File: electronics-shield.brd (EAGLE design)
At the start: 132 x 70 mm, 5 parts

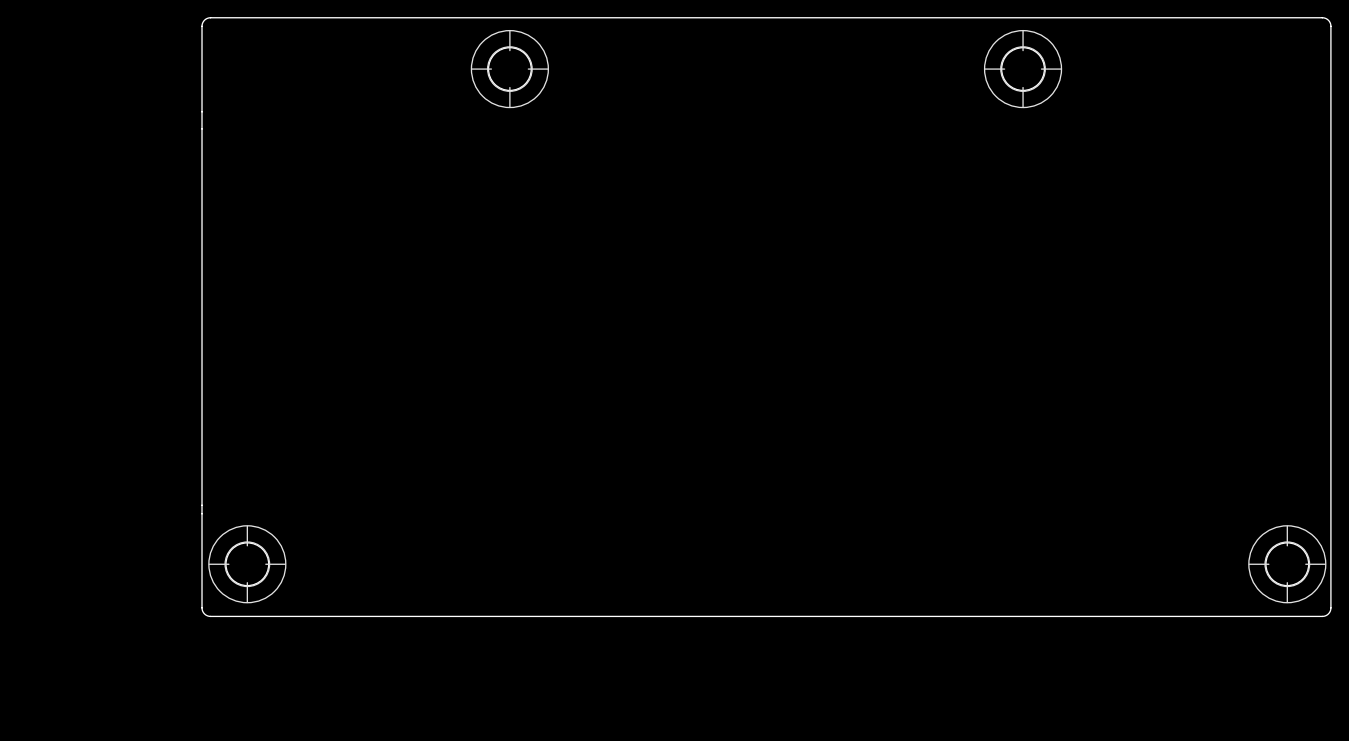
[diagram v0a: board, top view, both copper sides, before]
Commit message: H-Bridge change from L298P to TLE9201S, better wiring
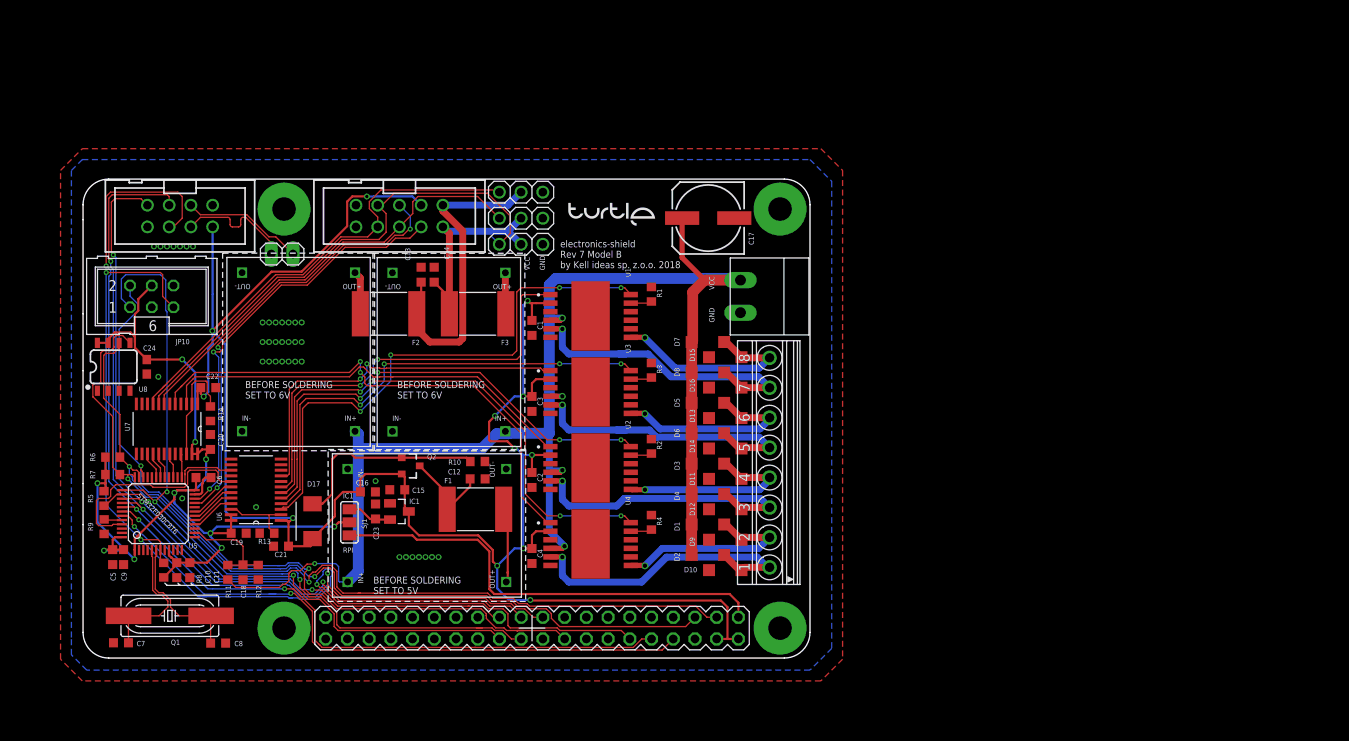
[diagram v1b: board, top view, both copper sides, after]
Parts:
- removed U$2: (no value), FIBOX:AB_081607
- removed U$3, U$4, U$5, U$6: (no value), holes:5,0
- added C1, C11, C12, C13, C14, C19, C2, C20, C21, C22, C23, C3, C4, C6, C9: 100n, resistor:C0603K
- added C10: 1u, resistor:C0603K
- added C15: 4.7uF, resistor:C0603K
- added C16: 1uF, resistor:C0603K
- added C17: 100u, resistor:153CLV-0807
- added C18: 22u, resistor:C0603K
- added C24: 0.1uF, rcl:C0603
- added C5: 4u7, resistor:C0603K
- added C7, C8: 20p, resistor:C0603K
- added D1, D10, D11, D12, D13, D14, D15, D16, D2, D3, D4, D5, D6, D7, D8, D9: SK38SMA, diode:SOD123
- added D17: SMBJ5.0A-TR, diode:SMBJ
- added F1, F2, F3: SL125-33, polyfuse-smd_10:2920L
- added IC1: MCP1703CB, linear:SOT23
- added JP1: Listwa kołkowa 2.54mm prosta 1x2 (2pin), pinhead:1X02
- added JP10: gniazdo IDC męskie 6pin proste, con-harting-ml:ML6
- added JP2, JP3, JP4: Listwa kołkowa 2.54mm prosta 1x3 (3pin), Synergiczne:1X03
- added JP5: Listwa stykowa 2.54mm prosta 2x20 (40-pin), wydłużona, RASPBERRY_PI_Bplus-eagle5:2X20
- added JP6: gniazdo IDC męskie 10pin proste, con-3m:PAK100/2500-10
- added JP7: gniazdo IDC męskie 8pin proste, Simplex-Connectors:PAK100/2500-10
- added JP8: Listwa zaciskowa rozłączalna 3.81mm 2pin kątowe 90° gniazdo, con-phoenix-381_l:MC2
- added JP9: Listwa zaciskowa rozłączalna 3.50mm 8pin kątowe 90° gniazdo, con-phoenix-350:1751303
- added PCB1, PCB2, PCB3: Moduł przetwornicy DC-DC Step-down 4.5..28V --- regulowane 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, Kell Ideas:MP1584_MODULE
- added Q1: 8 MHz, crystal:HC49UP
- added Q2: MOSFET-PCHANNELSMD, User-Submitted:SOT23-3
- added R1, R2, R3, R4: 10k, rcl:R0603
- added R10: 100k, rcl:R0603
- added R11, R13, R14, R5, R8, R9: 10k, resistor:R0603
- added R12: 1k, resistor:R0603
- added R6, R7: 4k7, resistor:R0603
- added SJ1: Zworka cynowa, jumper:SJ_2
- added U1, U2, U3, U4: TLE9201SGAUMA1, Kell Ideas:PG-DSO-12-9
- added U5: STM32F051C8T, STM32F030:LQFP48
- added U6, U7: SN74LVC4245APWR, Texas Instruments_By_element14_Batch_1:SOP65P640X120-24N
- added U8: 24LC256, SparkFun-IC-Memory:SO08
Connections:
- new net +3V3: C10.1, C11.1, C19.1, C20.1, C24.1, C5.1, C6.1, C9.1, JP10.4, R5.2, R6.2, R7.2, R8.2, SJ1.2, U5.1, U5.24, U5.48, U5.9, U6.23, U6.24, U7.23, U7.24, U8.7, U8.8
- new net +5V: C1.1, C15.1, C2.1, C21.1, C22.1, C23.1, C3.1, C4.1, D17.C, IC1.3, JP5.2, JP5.4, JP6.3, JP7.2, Q2.2, U1.2, U2.2, U3.2, U4.2, U6.1, U7.1
- new net +5V_RAW: F1.2, PCB1.OUT1+1
- new net +7V/1: C13.1, F2.1, JP4.2, JP6.1
- new net +7V/1_RAW: F2.2, PCB2.OUT1+1
- new net +7V/2: C14.1, F3.2, JP2.2, JP3.2, JP6.2
- new net +7V/2_RAW: F3.1, PCB3.OUT1+1
- new net 3V3: JP5.17
- new net 3V3_RPI: JP5.1, SJ1.3
- new net 3V3_STABILIZED: C16.1, IC1.2, SJ1.1
- new net 5V_NOT_TRIMMED: C12.1, F1.1, Q2.3
- new net BAT_MEAS: C18.1, R11.1, R12.2, U5.14
- new net BOOT0: R9.2, U5.44
- new net D1-R3: D17.A, Q2.1, R10.2
- new net DATA_N: JP1.2, JP7.3
- new net DATA_P: JP1.1, JP7.4
- new net EN1: U1.12, U6.3
- new net EN1_UC: U5.16, U6.21
- new net EN2: U3.12, U6.4
- new net EN2_UC: U5.17, U6.20
- new net EN3: U2.12, U6.5
- new net EN3_UC: U5.18, U6.19
- new net EN4: U4.12, U6.6
- new net EN4_UC: U5.19, U6.18
- new net GND: C1.2, C10.2, C11.2, C12.2, C13.2, C14.2, C15.2, C16.2, C17.-, C18.2, C19.2, C2.2, C20.2, C21.2, C22.2, C23.2, C24.2, C3.2, C4.2, C5.2, C6.2, C7.1, C8.1, C9.2, D10.A, D11.A, D12.A, D13.A, D14.A, D15.A, D16.A, D9.A, IC1.1, JP10.3, JP2.3, JP3.3, JP4.3, JP5.14, JP5.20, JP5.25, JP5.30, JP5.34, JP5.39, JP5.6, JP5.9, JP6.10, JP6.9, JP7.1, JP7.8, JP8.1, PCB1.IN1-1, PCB1.OUT1-1, PCB2.IN1-1, PCB2.OUT1-1, PCB3.IN1-1, PCB3.OUT1-1, R1.1, R10.1, R12.1, R13.2, R14.2, R2.1, R3.1, R4.1, R9.1, U1.13, U1.6, U2.13, U2.6, U3.13, U3.6, U4.13, U4.6, U5.23, U5.47, U5.8, U6.11, U6.12, U6.13, U7.11, U7.12, U7.13, U8.2, U8.3, U8.4
- new net IN11: U1.1, U6.7
- new net IN11_UC: U5.45, U6.17
- new net IN12: U6.8
- new net IN12_UC: U6.16
- new net IN21: U3.1, U6.9
- new net IN21_UC: U5.32, U6.15
- new net IN22: U6.10
- new net IN22_UC: U6.14
- new net IN31: U2.1, U7.3
- new net IN31_UC: U5.25, U7.21
- new net IN32: U7.4
- new net IN32_UC: U7.20
- new net IN41: U4.1, U7.5
- new net IN41_UC: U5.27, U7.19
- new net IN42: U7.6
- new net IN42_UC: U7.18
- new net LED: U5.15
- new net MOT11: D16.C, D8.A, JP9.7, U1.5
- new net MOT12: D15.C, D7.A, JP9.8, U1.7
- new net MOT21: D14.C, D6.A, JP9.5, U3.5
- new net MOT22: D13.C, D5.A, JP9.6, U3.7
- new net MOT31: D12.C, D4.A, JP9.3, U2.5
- new net MOT32: D11.C, D3.A, JP9.4, U2.7
- new net MOT41: D10.C, D2.A, JP9.1, U4.5
- new net MOT42: D1.A, D9.C, JP9.2, U4.7
- new net N$1: R13.1, U6.2, U6.22
- new net N$2: R14.1, U7.2, U7.22
- new net N$3: U7.10
- new net N$4: U7.14
- new net N$8: JP10.6
- new net NRST: JP10.5, JP5.12, R8.1, U5.7
- new net OSCILATOR_N: C7.2, Q1.2, U5.5
- new net OSCILATOR_P: C8.2, Q1.1, U5.6
- new net RPI_CLK: JP5.23, JP7.7, U5.39
- new net RPI_MISO: JP5.21, JP7.5, U5.40
- new net RPI_MOSI: JP5.19, JP7.6, U5.41
- new net RPI_RXD: JP5.10, U5.42
- new net RPI_TXD: JP5.8, U5.43
- new net SCL: JP5.5, R7.1, U5.35, U8.6
- new net SCL_TX: JP6.5, U5.21
- new net SDA: JP5.3, R6.1, U5.36, U8.5
- new net SDA_RX: JP6.4, U5.22
- new net SEN1: U5.10
- new net SEN2: U5.11
- new net SEN3: U5.12
- new net SEN4: U5.13
- new net SERVO1: JP2.1, JP6.6, U7.7
- new net SERVO1_UC: U5.29, U7.17
- new net SERVO2: JP3.1, JP6.7, U7.8
- new net SERVO2_UC: U5.30, U7.16
- new net SERVO3: JP4.1, JP6.8, U7.9
- new net SERVO3_UC: U5.31, U7.15
- new net SPI1_NSS: JP5.24, R5.1, U5.38
- new net SWCLK: JP10.1, JP5.22, U5.37
- new net SWDIO: JP10.2, JP5.18, U5.34
- new net U5_DIS: R1.2, U1.11
- new net U6_DIS: R2.2, U2.11
- new net U7_DIS: R3.2, U3.11
- new net U8_DIS: R4.2, U4.11
- new net VCC: C17.+, D1.C, D2.C, D3.C, D4.C, D5.C, D6.C, D7.C, D8.C, JP8.2, PCB1.IN1+1, PCB2.IN1+1, PCB3.IN1+1, R11.2, U1.4, U2.4, U3.4, U4.4
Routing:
- net +5V: track 0.00 -> 225.1 mm, vias 0 -> 12
- net VCC: track 0.00 -> 212.5 mm, vias 0 -> 5
- net NRST: track 0.00 -> 120.4 mm, vias 0 -> 3
- net +3V3: track 0.00 -> 119.9 mm, vias 0 -> 10
- net RPI_MOSI: track 0.00 -> 110.6 mm, vias 0 -> 3
- net SDA: track 0.00 -> 103.8 mm, vias 0 -> 2
- net RPI_MISO: track 0.00 -> 100.3 mm, vias 0 -> 3
- net SCL: track 0.00 -> 96.9 mm, vias 0 -> 2
- net SWCLK: track 0.00 -> 92.8 mm, vias 0 -> 3
- net RPI_CLK: track 0.00 -> 91.2 mm, vias 0 -> 3
- net SWDIO: track 0.00 -> 88.0 mm, vias 0 -> 2
- net RPI_TXD: track 0.00 -> 74.9 mm, vias 0 -> 2
- net RPI_RXD: track 0.00 -> 71.6 mm, vias 0 -> 2
- net EN1: track 0.00 -> 64.4 mm, vias 0 -> 4
- net EN4: track 0.00 -> 63.9 mm, vias 0 -> 4
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- added copper zone on layer 1, net GND
- added copper zone on layer 16, net GND
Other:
- board size 132 x 70 mm -> 85 x 56 mm
- board text added: "+5V"
- board text added: "+7V/1"
- board text added: "+7V/2"
- board text added: "3v3"
- board text added: "BEFORE SOLDERING SET TO 5V"
- board text added: "BEFORE SOLDERING SET TO 6V"
- board text added: "CLK"
- board text added: "DATA+"
- board text added: "DATA-"
- board text added: "GND"
- board text added: "IC1"
- board text added: "M11"
- board text added: "M12"
- board text added: "M21"
- board text added: "M22"
- board text added: "M31"
- board text added: "M32"
- board text added: "M41"
- board text added: "M42"
- board text added: "MISO"
- board text added: "MOSI"
- board text added: "MOTOR CONNECTOR"
- board text added: "NC"
- board text added: "NRST"
- board text added: "PiHat Rev. 7"
- board text added: "Power connector"
- board text added: "RPI"
- board text added: "SCL/TX"
- board text added: "SDA/RX"
- board text added: "SERVO1"
- board text added: "SERVO2"
- board text added: "SERVO3"
- board text added: "SIG"
- board text added: "STM32F030C8T6"
- board text added: "SWCLK"
- board text added: "SWDIO"
- board text added: "TIM1"
- board text added: "TIM2"
- board text added: "TIM3"
- board text added: "VCC"
- board text added: "electronics-shield Rev 7 Model B by Kell ideas sp. z.o.o. 2018"

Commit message: changed base for 7.c
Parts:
- removed C21, C22, C23: 100n, resistor:C0603K
- removed C24: 0.1uF, rcl:C0603
- removed JP10: gniazdo IDC męskie 6pin proste, con-harting-ml:ML6
- removed JP4: Listwa kołkowa 2.54mm prosta 1x3 (3pin), Synergiczne:1X03
- removed JP5: Listwa stykowa 2.54mm prosta 2x20 (40-pin), wydłużona, RASPBERRY_PI_Bplus-eagle5:2X20
- removed JP6: gniazdo IDC męskie 10pin proste, con-3m:PAK100/2500-10
- removed JP7: gniazdo IDC męskie 8pin proste, Simplex-Connectors:PAK100/2500-10
- removed JP8: Listwa zaciskowa rozłączalna 3.81mm 2pin kątowe 90° gniazdo, con-phoenix-381_l:MC2
- removed JP9: Listwa zaciskowa rozłączalna 3.50mm 8pin kątowe 90° gniazdo, con-phoenix-350:1751303
- removed PCB2, PCB3: Moduł przetwornicy DC-DC Step-down 4.5..28V --- regulowane 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, Kell Ideas:MP1584_MODULE
- removed R14: 10k, resistor:R0603
- removed U5: STM32F051C8T, STM32F030:LQFP48
- removed U6, U7: SN74LVC4245APWR, Texas Instruments_By_element14_Batch_1:SOP65P640X120-24N
- removed U8: 24LC256, SparkFun-IC-Memory:SO08
- added $3_0_$_2018-08-14_21-12-08, $3_1_$_2018-08-14_21-12-08, $3_2_$_2018-08-14_21-12-08: Moduł przetwornicy DC-DC Step-down 4.5..28V --- regulowane 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, Kell Ideas:DC-BRICK
- added IC2: TLE9201SG, Kell Ideas:PG-DSO-12-9
- added IC5: LINEAR_MCP1703CB, electronics-shield:LINEAR_SOT23
- added J1: USB-MICRO-B, Kell Ideas:USB-MICRO-B
- added LED1, LED2, LED3, LED4, LED5: LEDCHIPLED_0603, audio amplifier example:CHIPLED_0603
- added Q3: ON-SEMICONDUCTOR---NTZD3154NT1G_ON_SEMICONDUCTOR_NTZD3154NT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, electronics-shield:ON-SEMICONDUCTOR---NTZD3154NT1G_ON_SEMICONDUCTOR_NTZD3154NT1G_0
- added RN1, RN2: 1k, SparkFun-Resistors:0805-ARV
- added SJ2: (no value), Kell Ideas:SJ
- added SV1: gniazdo IDC męskie 6pin proste, Kell Ideas:ML6
- added SV2: (no value), Kell Ideas:ML10
- added SV3: ML8, Kell Ideas:ML8
- added X1: CONNECTOR_PHOENIX_3.81, Kell Ideas:3.81MM_2PIN
- added X2: Listwa zaciskowa rozłączalna 3.50mm 8pin kątowe 90° gniazdo, Kell Ideas:3.5MM_8PIN
- added Y1: 8 MHz, Kell Ideas:HC49UP
- C1, C10, C11, C12, C13, C14, C15, C16, C18, C19, C2, C3, C4, C5, C6, C7, C8, C9: device resistor:C0603K -> Kell Ideas:C0603K
- C17: device resistor:153CLV-0807 -> Kell Ideas:FI8_6.2
- C20: value 100n -> 0.1uF; device resistor:C0603K -> Kell Ideas:C0603K
- D1, D10, D11, D12, D13, D14, D15, D16, D2, D3, D4, D5, D6, D7, D8, D9: device diode:SOD123 -> Kell Ideas:SOD123
- D17: device diode:SMBJ -> Kell Ideas:SMBJ
- F1, F2, F3: device polyfuse-smd_10:2920L -> Kell Ideas:FUSC7351X125
- IC1: value MCP1703CB -> TLE9201SG; device linear:SOT23 -> Kell Ideas:PG-DSO-12-9
- IC3, IC4: value TLE9201SGAUMA1 -> TLE9201SG
- JP1: value Listwa kołkowa 2.54mm prosta 1x2 (2pin) -> Listwa kołkowa 2.54mm prosta 1x3 (3pin); device pinhead:1X02 -> Kell Ideas:1X03_ROUND_DNP
- JP2, JP3: device Synergiczne:1X03 -> Kell Ideas:1X03_ROUND_DNP
- PCB1: value Moduł przetwornicy DC-DC Step-down 4.5..28V --- regulowane 0.8..20V MP1584 -> Listwa stykowa 2.54mm prosta 2x20 (40-pin), wydłużona; device Kell Ideas:MP1584_MODULE -> Kell Ideas:RASPBERRY_PI_B+_CONNECTOR
- Q1: value 8 MHz -> USER-SUBMITTED_MOSFET-PCHANNELSMD; device crystal:HC49UP -> electronics-shield:USER-SUBMITTED_SOT23-3
- Q2: value MOSFET-PCHANNELSMD -> ON-SEMICONDUCTOR---NTZD3154NT1G_ON_SEMICONDUCTOR_NTZD3154NT1GON_SEMICONDUCTOR_NTZD3154NT1G_0_0; device User-Submitted:SOT23-3 -> electronics-shield:ON-SEMICONDUCTOR---NTZD3154NT1G_ON_SEMICONDUCTOR_NTZD3154NT1G_0
- R1, R4: device rcl:R0603 -> Kell Ideas:R0603
- R10: value 100k -> 330; device rcl:R0603 -> Kell Ideas:R0603
- R11: value 10k -> 330; device resistor:R0603 -> Kell Ideas:R0603
- R12: value 1k -> 200; device resistor:R0603 -> Kell Ideas:R0603
- R13: value 10k -> 200; device resistor:R0603 -> Kell Ideas:R0603
- R2, R3: value 10k -> 4k7; device rcl:R0603 -> Kell Ideas:R0603
- R5: device resistor:R0603 -> Kell Ideas:R0603
- R6: value 4k7 -> 100k; device resistor:R0603 -> Kell Ideas:R0603
- R7: value 4k7 -> 10k; device resistor:R0603 -> Kell Ideas:R0603
- R8: value 10k -> 1k; device resistor:R0603 -> Kell Ideas:R0603
- R9: value 10k -> 1.5k; device resistor:R0603 -> Kell Ideas:R0603
- SJ1: value Zworka cynowa -> (none); device jumper:SJ_2 -> Kell Ideas:SJ
- U1: value TLE9201SGAUMA1 -> STM32F0XX8T; device Kell Ideas:PG-DSO-12-9 -> Kell Ideas:LQFP48
- U2: value TLE9201SGAUMA1 -> EEPROM-I2C; device Kell Ideas:PG-DSO-12-9 -> Kell Ideas:SO-08
- moved R9 83.5 mm to (79.5, 48.0), turned to 180 degrees
- moved PCB1 74.2 mm to (85.1, 56.1), turned to 180 degrees
- moved R1 68.3 mm to (2.54, 18.8), turned to 90 degrees
- moved R4 57.3 mm to (9.53, 10.4)
- moved R2 57.0 mm to (10.4, 34.5), turned to 0 degrees
- moved R3 56.2 mm to (10.4, 36.6), turned to 0 degrees
- moved U1 55.6 mm to (8.89, 17.0), turned to 0 degrees
- moved R12 52.4 mm to (72.9, 8.38), turned to 180 degrees
- moved U2 48.1 mm to (12.0, 30.6), turned to 90 degrees
- moved R6 42.7 mm to (46.2, 23.1)
- moved R11 37.0 mm to (25.1, 46.2), turned to 0 degrees
- moved R10 33.6 mm to (21.8, 46.2), turned to 0 degrees
- moved Q1 33.1 mm to (38.4, 22.6), turned to 270 degrees
- moved IC1 32.0 mm to (59.4, 40.1)
- moved JP1 28.3 mm to (51.3, 51.6)
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- renumbered U3 to IC3, U4 to IC4
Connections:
- removed net EN1_UC: U5.16, U6.21
- removed net EN2_UC: U5.17, U6.20
- removed net EN3_UC: U5.18, U6.19
- removed net EN4_UC: U5.19, U6.18
- removed net IN11_UC: U5.45, U6.17
- removed net IN12: U6.8
- removed net IN12_UC: U6.16
- removed net IN21_UC: U5.32, U6.15
- removed net IN22: U6.10
- removed net IN22_UC: U6.14
- removed net IN31_UC: U5.25, U7.21
- removed net IN32: U7.4
- removed net IN32_UC: U7.20
- removed net IN41_UC: U5.27, U7.19
- removed net IN42: U7.6
- removed net IN42_UC: U7.18
- removed net U5_DIS: R1.2, U1.11
- removed net U6_DIS: R2.2, U2.11
- removed net U7_DIS: IC3.11, R3.2
- removed net U8_DIS: IC4.11, R4.2
- new net N$14: Q2.4, RN2.3
- new net N$16: Q2.3, RN2.4
- new net N$5: LED5.C, R13.1
- new net SO1-SI3: IC1.3, IC3.8
- new net SO2-SI4: IC2.3, IC4.8
- new net SO3-SI2: IC2.8, IC3.3
- new net TLE_NSS: IC1.9, IC2.9, IC3.9, IC4.9, U1.20
- net +3V3: now also C1.1, C2.1, C3.1, C4.1, IC1.2, IC2.2, IC3.2, IC4.2, LED5.A, Q2.2, Q2.5, Q3.2, Q3.5, R1.2, R2.2, R3.2, R4.2, RN1.6, RN1.8, RN2.6, RN2.8, SJ1.1, SJ2.1, SV1.4, U1.1, U1.24, U1.48, U1.9, U2.7, U2.8; no longer C19.1, C24.1, JP10.4, R5.2, R6.2, R7.2, R8.2, SJ1.2, U5.1, U5.24, U5.48, U5.9, U6.23, U6.24, U7.23, U7.24, U8.7, U8.8
- net +5V: now also C19.1, IC5.3, LED4.A, PCB1.2, PCB1.4, Q1.2, RN1.5, RN1.7, RN2.5, RN2.7, SV2.3, SV3.2; no longer C1.1, C2.1, C21.1, C22.1, C23.1, C3.1, C4.1, IC1.3, IC3.2, IC4.2, JP5.2, JP5.4, JP6.3, JP7.2, Q2.2, U1.2, U2.2, U6.1, U7.1
- net +5V_RAW: now also $3_0_$_2018-08-14_21-12-08.OUT1+1; no longer PCB1.OUT1+1
- net +7V/1: now also JP3.2, LED2.A, SV2.1; no longer JP4.2, JP6.1
- net +7V/1_RAW: now also $3_1_$_2018-08-14_21-12-08.OUT1+1; no longer PCB2.OUT1+1
- net +7V/2: now also JP1.2, LED3.A, SV2.2; no longer JP3.2, JP6.2
- net +7V/2_RAW: now also $3_2_$_2018-08-14_21-12-08.OUT1+1; no longer PCB3.OUT1+1
- net 3V3: now also PCB1.17; no longer JP5.17
- net 3V3_RPI: now also PCB1.1, SJ2.2; no longer JP5.1, SJ1.3
- net 3V3_STABILIZED: now also IC5.2, SJ1.2; no longer IC1.2, SJ1.1
- net 5V_NOT_TRIMMED: now also Q1.3; no longer Q2.3
- net BAT_MEAS: now also R7.1, R8.2, U1.14; no longer R11.1, R12.2, U5.14
- net BOOT0: now also R5.2, U1.44; no longer R9.2, U5.44
- net D1-R3: now also Q1.1, R6.2; no longer Q2.1, R10.2
- net DATA_N: now also J1.D-, SV3.3; no longer JP1.2, JP7.3
- net DATA_P: now also J1.D+, SV3.4; no longer JP1.1, JP7.4
- net EN1: now also IC1.12, U1.16; no longer U1.12, U6.3
- net EN2: now also U1.17; no longer U6.4
- net EN3: now also IC2.12, U1.18; no longer U2.12, U6.5
- net EN4: now also U1.19; no longer U6.6
- net GND: now also $3_0_$_2018-08-14_21-12-08.IN1-1, $3_0_$_2018-08-14_21-12-08.OUT1-1, $3_1_$_2018-08-14_21-12-08.IN1-1, $3_1_$_2018-08-14_21-12-08.OUT1-1, $3_2_$_2018-08-14_21-12-08.IN1-1, $3_2_$_2018-08-14_21-12-08.OUT1-1, D10.2, D11.2, D12.2, D13.2, D14.2, D15.2, D16.2, D9.2, IC1.11, IC1.13, IC1.6, IC2.11, IC2.13, IC2.6, IC3.11, IC4.11, IC5.1, J1.GND, J1.SHIELD$1, J1.SHIELD$2, J1.SHIELD$3, J1.SHIELD$4, JP1.3, PCB1.14, PCB1.20, PCB1.25, PCB1.30, PCB1.34, PCB1.39, PCB1.6, PCB1.9, R10.2, R11.2, R12.2, R5.1, R6.1, R8.1, R9.2, SV1.3, SV2.10, SV2.9, SV3.1, SV3.8, U1.23, U1.47, U1.8, U2.2, U2.3, U2.4, X1.1; no longer C21.2, C22.2, C23.2, C24.2, D10.A, D11.A, D12.A, D13.A, D14.A, D15.A, D16.A, D9.A, IC1.1, JP10.3, JP4.3, JP5.14, JP5.20, JP5.25, JP5.30, JP5.34, JP5.39, JP5.6, JP5.9, JP6.10, JP6.9, JP7.1, JP7.8, JP8.1, PCB1.IN1-1, PCB1.OUT1-1, PCB2.IN1-1, PCB2.OUT1-1, PCB3.IN1-1, PCB3.OUT1-1, R1.1, R10.1, R12.1, R14.2, R2.1, R3.1, R4.1, R9.1, U1.13, U1.6, U2.13, U2.6, U5.23, U5.47, U5.8, U6.11, U6.12, U6.13, U7.11, U7.12, U7.13, U8.2, U8.3, U8.4
- net IN11: now also IC1.1, U1.45; no longer U1.1, U6.7
- net IN21: now also U1.32; no longer U6.9
- net IN31: now also IC2.1, U1.25; no longer U2.1, U7.3
- net IN41: now also U1.27; no longer U7.5
- net LED: now also U1.15; no longer U5.15
- net MOT11: now also D16.1, D8.2, IC1.5, X2.7; no longer D16.C, D8.A, JP9.7, U1.5
- net MOT12: now also D15.1, D7.2, IC1.7, X2.8; no longer D15.C, D7.A, JP9.8, U1.7
- net MOT21: now also D14.1, D6.2, X2.5; no longer D14.C, D6.A, JP9.5
- net MOT22: now also D13.1, D5.2, X2.6; no longer D13.C, D5.A, JP9.6
- net MOT31: now also D12.1, D4.2, IC2.5, X2.3; no longer D12.C, D4.A, JP9.3, U2.5
- net MOT32: now also D11.1, D3.2, IC2.7, X2.4; no longer D11.C, D3.A, JP9.4, U2.7
- net MOT41: now also D10.1, D2.2, X2.1; no longer D10.C, D2.A, JP9.1
- net MOT42: now also D1.2, D9.1, X2.2; no longer D1.A, D9.C, JP9.2
- net N$1: now also LED1.C, R9.1; no longer R13.1, U6.2, U6.22
- net N$2: now also LED2.C, R10.1; no longer R14.1, U7.2, U7.22
- net N$3: now also LED3.C, R11.1; no longer U7.10
- net N$4: now also LED4.C, R12.1; no longer U7.14
- net N$8: now also SV1.6; no longer JP10.6
- net NRST: now also PCB1.12, R4.1, SV1.5, U1.7; no longer JP10.5, JP5.12, R8.1, U5.7
- net OSCILATOR_N: now also U1.5, Y1.2; no longer Q1.2, U5.5
- net OSCILATOR_P: now also U1.6, Y1.1; no longer Q1.1, U5.6
- net RPI_CLK: now also IC1.10, IC2.10, IC3.10, IC4.10, PCB1.23, SV3.7, U1.39; no longer JP5.23, JP7.7, U5.39
- net RPI_MISO: now also IC4.3, PCB1.21, SV3.5, U1.40; no longer JP5.21, JP7.5, U5.40
- net RPI_MOSI: now also IC1.8, PCB1.19, SV3.6, U1.41; no longer JP5.19, JP7.6, U5.41
- net RPI_RXD: now also PCB1.10, U1.42; no longer JP5.10, U5.42
- net RPI_TXD: now also PCB1.8, U1.43; no longer JP5.8, U5.43
- net SCL: now also PCB1.5, R3.1, U1.35, U2.6; no longer JP5.5, R7.1, U5.35, U8.6
- net SCL_TX: now also SV2.5, U1.21; no longer JP6.5, U5.21
- net SDA: now also PCB1.3, R2.1, U1.36, U2.5; no longer JP5.3, R6.1, U5.36, U8.5
- net SDA_RX: now also SV2.4, U1.22; no longer JP6.4, U5.22
- net SEN1: now also U1.10; no longer U5.10
- net SEN2: now also U1.11; no longer U5.11
- net SEN3: now also U1.12; no longer U5.12
- net SEN4: now also U1.13; no longer U5.13
- net SERVO1: now also JP1.1, Q3.3, RN1.4, SV2.6; no longer JP2.1, JP6.6, U7.7
- net SERVO1_UC: now also Q3.4, RN1.3, U1.29; no longer U5.29, U7.17
- net SERVO2: now also JP2.1, Q3.6, RN1.2, SV2.7; no longer JP3.1, JP6.7, U7.8
- net SERVO2_UC: now also Q3.1, RN1.1, U1.30; no longer U5.30, U7.16
- net SERVO3: now also JP3.1, Q2.6, RN2.2, SV2.8; no longer JP4.1, JP6.8, U7.9
- net SERVO3_UC: now also Q2.1, RN2.1, U1.31; no longer U5.31, U7.15
- net SPI1_NSS: now also PCB1.24, R1.1, U1.38; no longer JP5.24, R5.1, U5.38
- net SWCLK: now also PCB1.22, SV1.1, U1.37; no longer JP10.1, JP5.22, U5.37
- net SWDIO: now also PCB1.18, SV1.2, U1.34; no longer JP10.2, JP5.18, U5.34
- net VCC: now also $3_0_$_2018-08-14_21-12-08.IN1+1, $3_1_$_2018-08-14_21-12-08.IN1+1, $3_2_$_2018-08-14_21-12-08.IN1+1, D1.1, D2.1, D3.1, D4.1, D5.1, D6.1, D7.1, D8.1, IC1.4, IC2.4, LED1.A, R7.2, X1.2; no longer D1.C, D2.C, D3.C, D4.C, D5.C, D6.C, D7.C, D8.C, JP8.2, PCB1.IN1+1, PCB2.IN1+1, PCB3.IN1+1, R11.2, U1.4, U2.4
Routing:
- net +3V3: track 119.9 -> 258.0 mm, vias 10 -> 22
- net TLE_NSS: track 0.00 -> 118.1 mm, vias 0 -> 10
- net RPI_CLK: track 91.2 -> 160.1 mm, vias 3 -> 10
- net RPI_MOSI: track 110.6 -> 160.1 mm, vias 3 -> 4
- net +5V: track 225.1 -> 180.3 mm
- net +7V/1: track 38.2 -> 69.7 mm
- net +7V/2: track 27.1 -> 56.0 mm, vias 0 -> 1
- net SERVO1_UC: track 3.02 -> 30.8 mm, vias 0 -> 2
- net IN11: track 51.5 -> 78.6 mm
- net IN11_UC: track 26.2 -> 0.00 mm
- net SERVO2_UC: track 3.09 -> 28.6 mm
- net SPI1_NSS: track 55.6 -> 80.4 mm, vias 2 -> 3
- net SERVO3_UC: track 3.16 -> 24.3 mm
- net SO1-SI3: track 0.00 -> 20.1 mm
- net SO2-SI4: track 0.00 -> 19.6 mm
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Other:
- board text added: "3V3"
- board text added: "5V"
- board text added: "7V/1"
- board text added: "7V/2"
- board text added: "electronics-shield ver 7 rev C 2018 Kell ideas Ltd."
- board text removed: "electronics-shield Rev 7 Model B by Kell ideas sp. z.o.o. 2018"

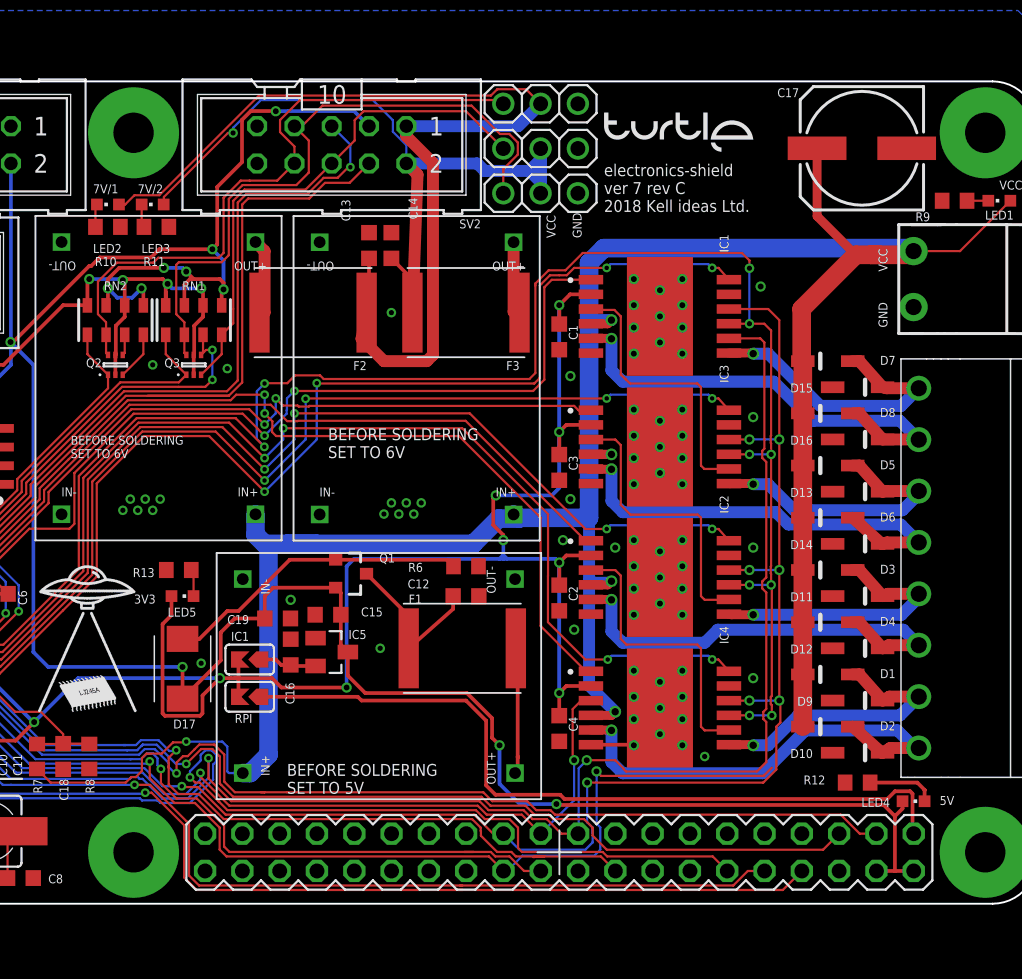
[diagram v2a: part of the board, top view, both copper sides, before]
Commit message: Added place to solder additional DC/DC converter, removed PTC from serwo power lines
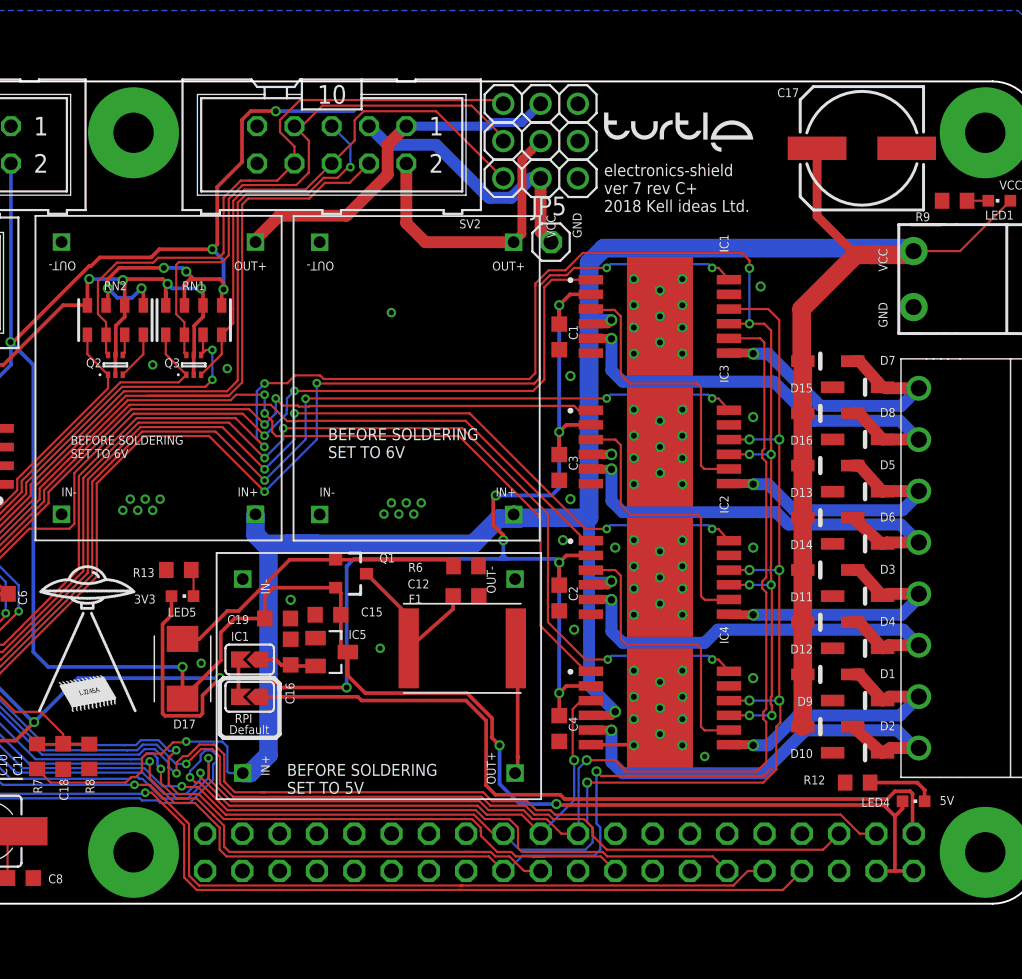
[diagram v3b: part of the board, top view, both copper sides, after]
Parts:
- removed C13, C14: 100n, Kell Ideas:C0603K
- removed F2, F3: SL125-33, Kell Ideas:FUSC7351X125
- removed LED2, LED3: LEDCHIPLED_0603, audio amplifier example:CHIPLED_0603
- removed R10, R11: 330, Kell Ideas:R0603
- added JP5: (no value), pinhead:1X01
- moved JP2 3.56 mm to (51.3, 52.1)
- moved JP1 2.03 mm to (51.3, 49.5)
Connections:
- removed net +7V/1_RAW: $3_1_$_2018-08-14_21-12-08.OUT1+1, F2.2
- removed net +7V/2_RAW: $3_2_$_2018-08-14_21-12-08.OUT1+1, F3.1
- removed net N$2: LED2.C, R10.1
- removed net N$3: LED3.C, R11.1
- new net +5V/2: JP1.2, JP5.1, SV2.3
- net +5V: no longer SV2.3
- net +7V/1: now also $3_1_$_2018-08-14_21-12-08.OUT1+1; no longer C13.1, F2.1, LED2.A
- net +7V/2: now also $3_2_$_2018-08-14_21-12-08.OUT1+1; no longer C14.1, F3.2, JP1.2, LED3.A
- net GND: no longer C13.2, C14.2, R10.2, R11.2
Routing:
- net +7V/1: track 69.7 -> 24.6 mm
- net +7V/2: track 56.0 -> 19.6 mm, vias 1 -> 0
- net +5V/2: track 0.00 -> 18.9 mm
- net +7V/1_RAW: track 5.41 -> 0.00 mm
- net +7V/2_RAW: track 5.15 -> 0.00 mm
- net SERVO2: track 44.6 -> 39.8 mm
- net N$3: track 1.59 -> 0.00 mm
- net N$2: track 1.57 -> 0.00 mm
- net +5V: track 180.3 -> 178.9 mm
- net SERVO1: track 35.5 -> 36.4 mm
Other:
- board text added: "Default"
- board text added: "electronics-shield ver 7 rev C+ 2018 Kell ideas Ltd."
- board text removed: "7V/1"
- board text removed: "7V/2"
- board text removed: "electronics-shield ver 7 rev C 2018 Kell ideas Ltd."

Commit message: 7C+ release
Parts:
- JP5: value (none) -> Listwa kołkowa 2.54mm prosta 1x1 (1pin)
- Q2, Q3: value ON-SEMICONDUCTOR---NTZD3154NT1G_ON_SEMICONDUCTOR_NTZD3154NT1GON_SEMICONDUCTOR_NTZD3154NT1G_0_0 -> NTZD3154NT1G
- SV1: value gniazdo IDC męskie 6pin proste -> Gniazdo IDC męskie 6pin proste
- SV2: value (none) -> Gniazdo IDC męskie 10pin proste
- SV3: value ML8 -> Gniazdo IDC męskie 8pin proste
- renumbered $3_0_$_2018-08-14_21-12-08 to IC6, $3_1_$_2018-08-14_21-12-08 to IC7, $3_2_$_2018-08-14_21-12-08 to IC8
